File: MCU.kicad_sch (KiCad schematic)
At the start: 87 parts, among them IC1 MT2492, J1 FH34SRJ-8S-0.5SH_50_, SW1 TS-1088-AR02016, U1 USBLC6-2SC6, U3 ATSAMD51J19A-A, U4 ESP32-C3-MINI-1-H4X, U5 TLV75733PDBV

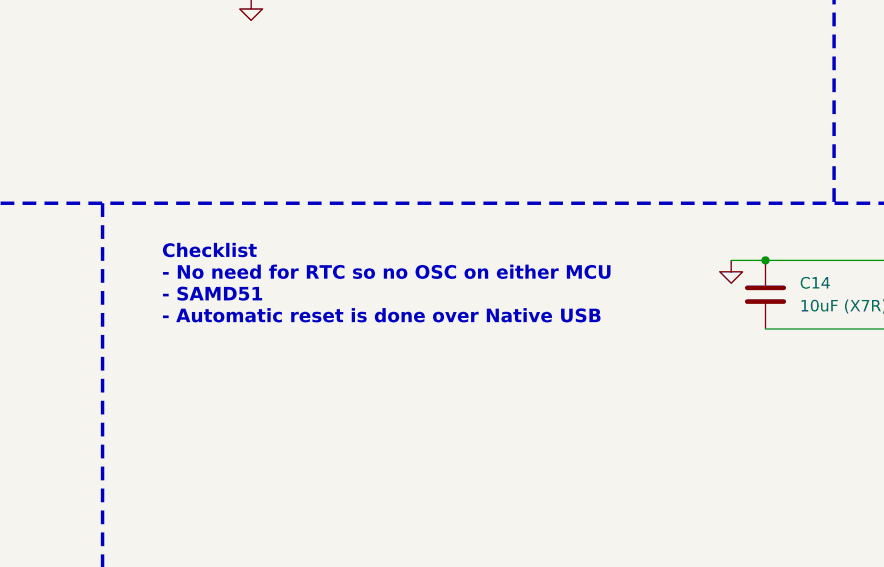
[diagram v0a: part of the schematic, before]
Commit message: Add SAMD51 pin planner and LFR torque calculator tools
Move samd51-pin-planner.html into Tools/ alongside a new
lfr-torque-calculator.html and its SAMD51A19J.json pin/peripheral
data source. Also ignore KiCad's transient *.lck files going forward.

Minor schematic touch-ups: corrected a resistor value typo in
SENSOR_ARRAY (47Ω, was mislabeled Ω-less) and updated the MCU
checklist note to reflect open questions (peripheral mux, current
sensing) instead of a stale done item.

Co-Authored-By: Claude Sonnet 5 <noreply@anthropic.com>
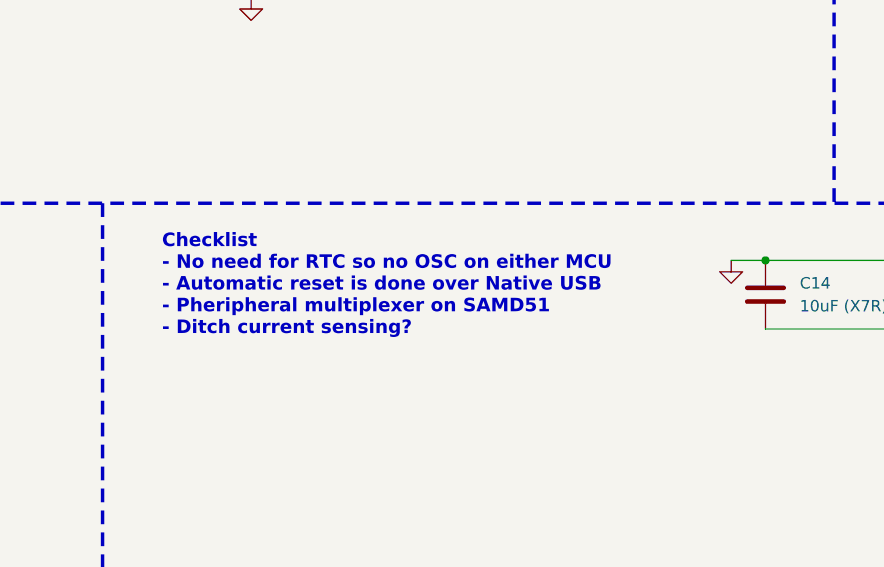
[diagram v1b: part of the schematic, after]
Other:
- note added: "Checklist - No need for RTC so no OSC on either MCU - Automatic reset is done over Native USB - Pheripheral multiplexer on SAMD51 - Ditch current sensing?"
- note removed: "Checklist - No need for RTC so no OSC on either MCU - SAMD51 - Automatic reset is done over Native USB"
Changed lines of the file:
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@@
 		)
 	)
-	(text "Checklist\n- No need for RTC so no OSC on either MCU\n- SAMD51\n- Automatic reset is done over Native USB"
+	(text "Checklist\n- No need for RTC so no OSC on either MCU\n- Automatic reset is done over Native USB\n- Pheripheral multiplexer on SAMD51\n- Ditch current sensing?\n"
 		(exclude_from_sim no)
 		(at 100.584 92.964 0)

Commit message: Remove INA240 current sensing from motor drive
Drop both INA240A1DR current-sense amplifiers and their support
passives from the DRV8874 motor drive circuit, along with the
associated SENSE_IN/C_SENSE nets and "MOTOR CURRENT SENSING"
annotation. This was flagged as an open question on the MCU
checklist; decided to simplify rather than keep it.

Co-Authored-By: Claude Sonnet 5 <noreply@anthropic.com>
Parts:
- removed C1, C2: 100nF/50V, Capacitor_SMD:C_0402_1005Metric, symbol Device:C
- removed C3, C4: 2.2uF/16V, Capacitor_SMD:C_0402_1005Metric, symbol Device:C
- removed INAA1, INAB1: INA240A1DR, SAVITAR:SOIC127P600X175-8N, symbol SAVITAR:INA240A1DR
- removed SHUNT1, SHUNT2: 50mΩ, Resistor_SMD:R_0805_2012Metric, symbol Device:R_US
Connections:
- no-connect marks 81 -> 79
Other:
- note removed: "1.5A × 0.050Ω = 75mV 75mV × 20 = 1.5V"
- note removed: "MOTOR CURRENT SENSING"
- moved on the sheet: C14, C16, C22, C23, C24, C25, C27, C32, C35, C36, C38, C49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
